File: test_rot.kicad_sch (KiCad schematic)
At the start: 37 parts, among them J1 1S 1P +ve, J10 1S 1P +ve, J11 1S 1P -ve, J12 1S 3P +ve, J13 1S 3P -ve, J14 1S 4P +ve, J15 1S 4P -ve, J16 1S 2P +ve, J17 1S 2P -ve, J18 1S 1P -ve, J19 2S 1P -ve, J2 1S 1P -ve, J20 3S 1P -ve, J3 4S B +ve, J4 4S B -ve, J5 4P B +ve, J6 4P B -ve, J7 2S 1P +ve, J8 3S 1P +ve, J9 4S 1P +ve

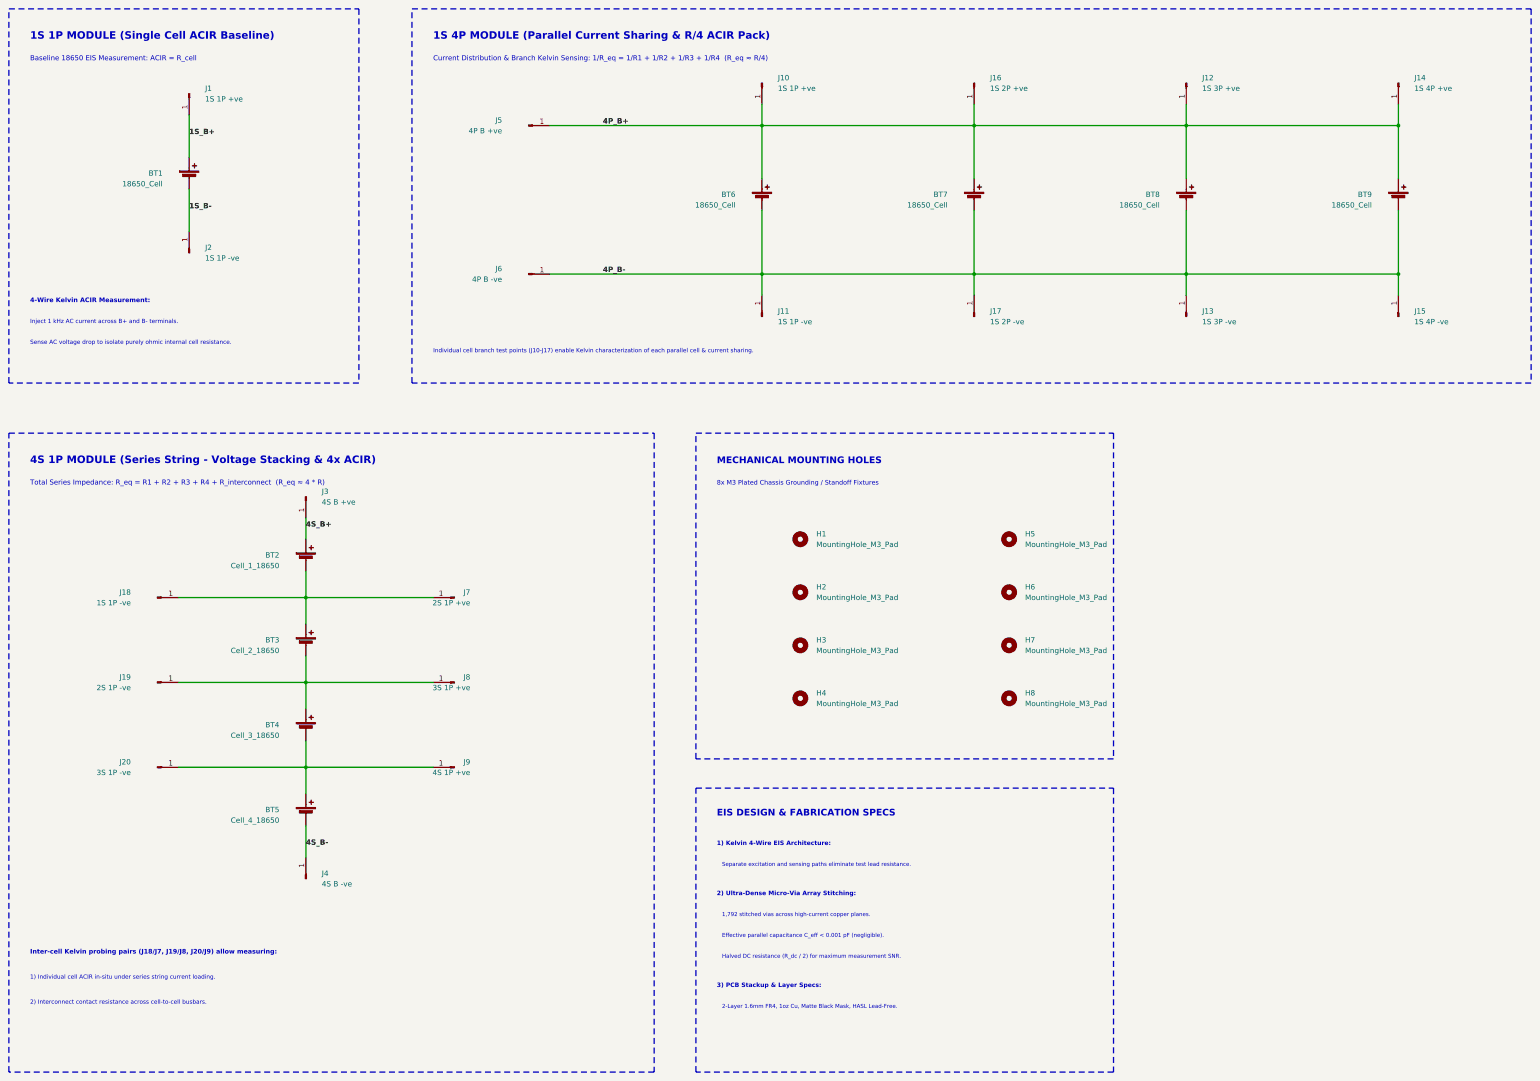
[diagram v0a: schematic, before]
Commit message: test: add test schematics, ERC reports, and verification artifacts for ACIR PCB
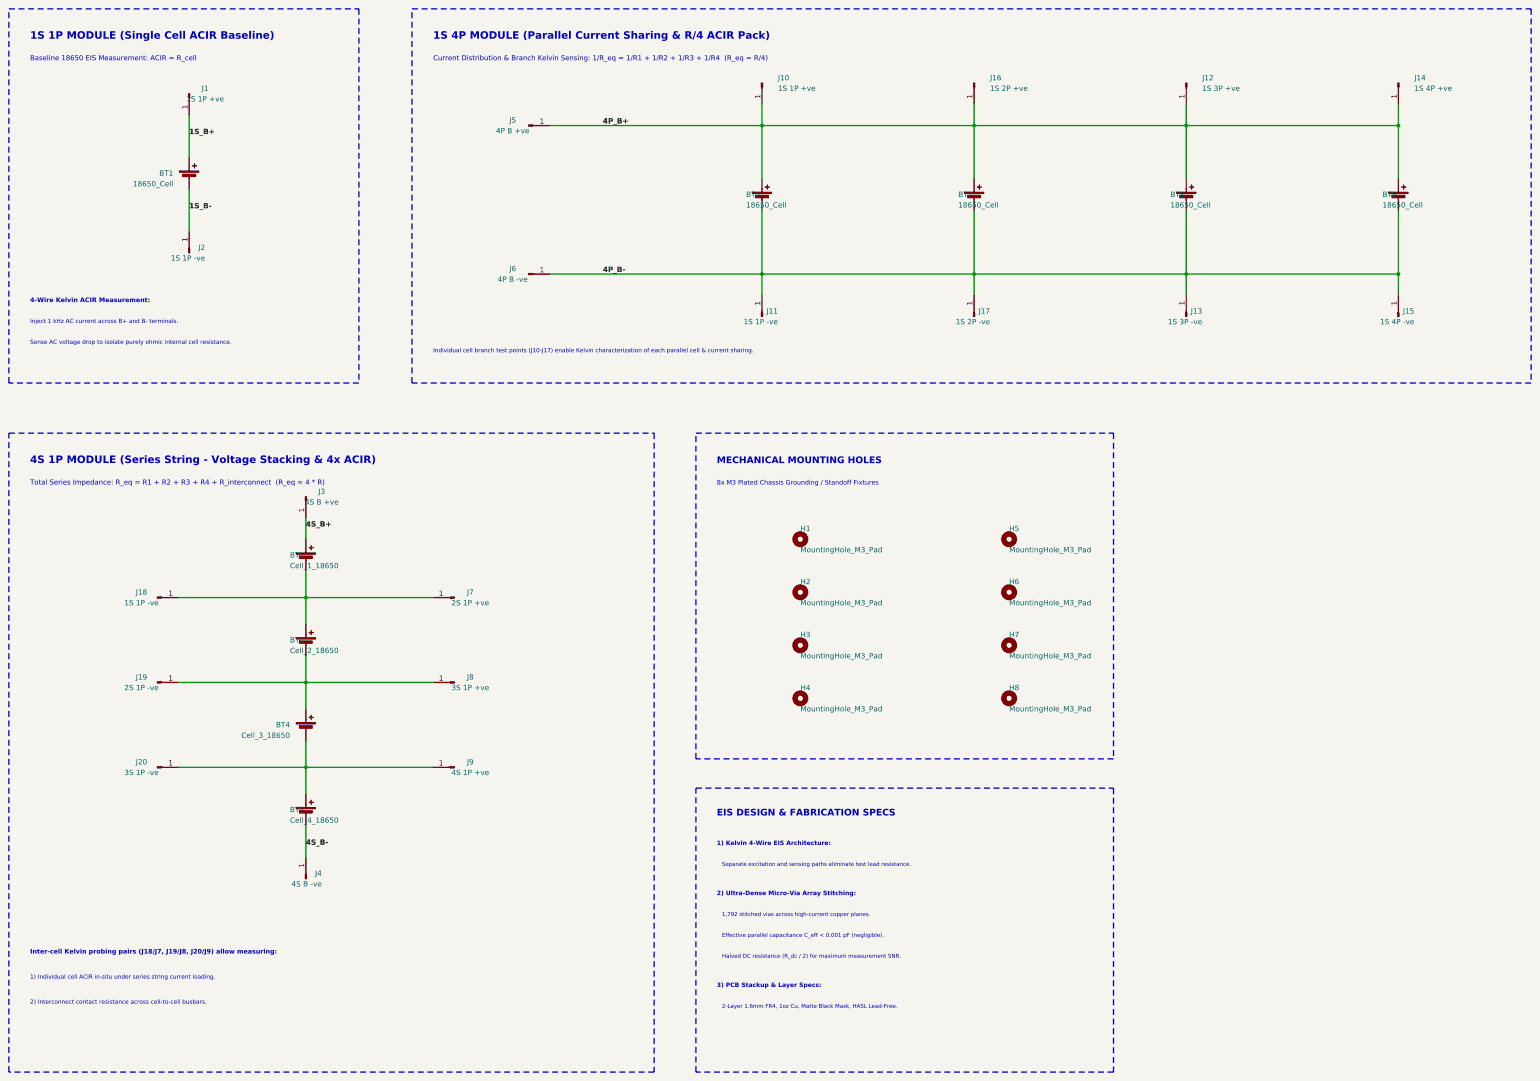
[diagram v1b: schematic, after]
